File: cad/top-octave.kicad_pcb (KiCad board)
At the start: 2 copper layers, 21 parts, among them J1 DIP-16, U1 ATtiny4-TS, U10 ATtiny4-TS, U11 ATtiny4-TS, U12 ATtiny4-TS, U13 ATtiny4-TS, U2 ATtiny4-TS, U3 ATtiny4-TS, U4 ATtiny4-TS, U5 ATtiny4-TS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

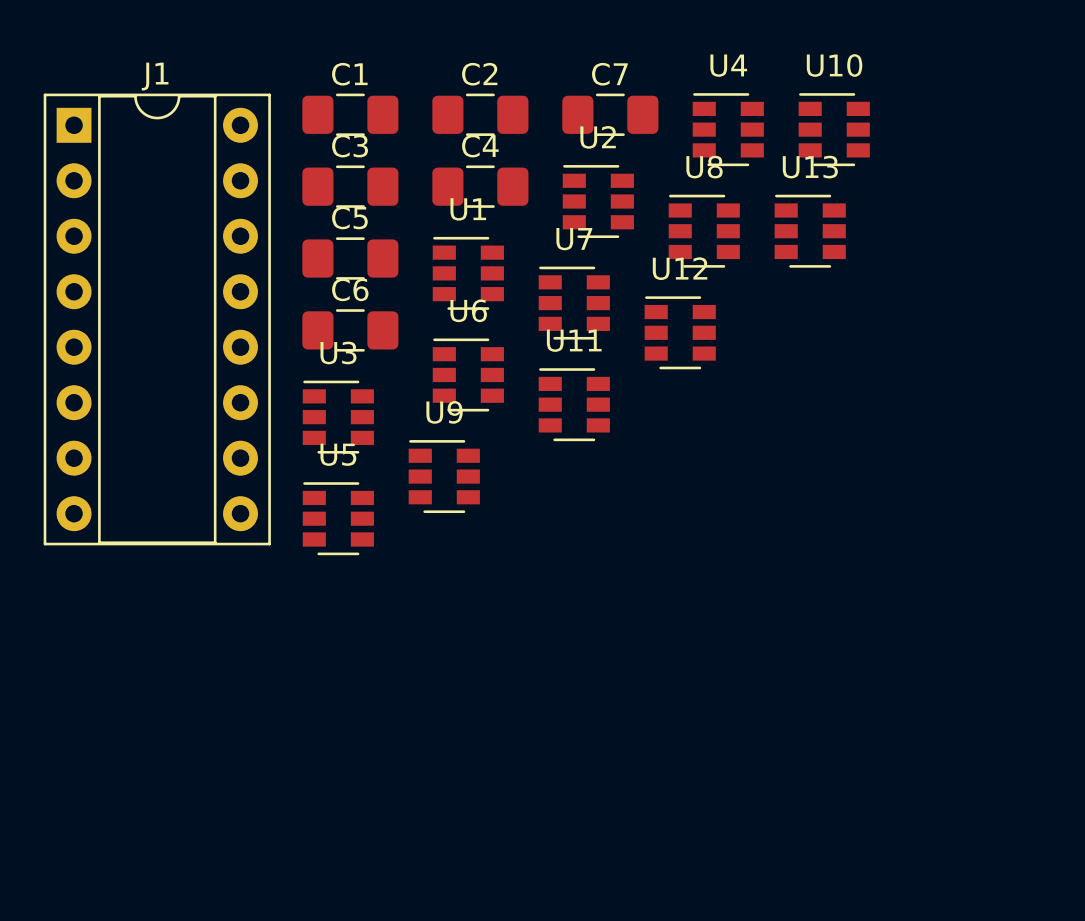
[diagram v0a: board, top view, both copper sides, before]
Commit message: Fix wrong header for MK50242
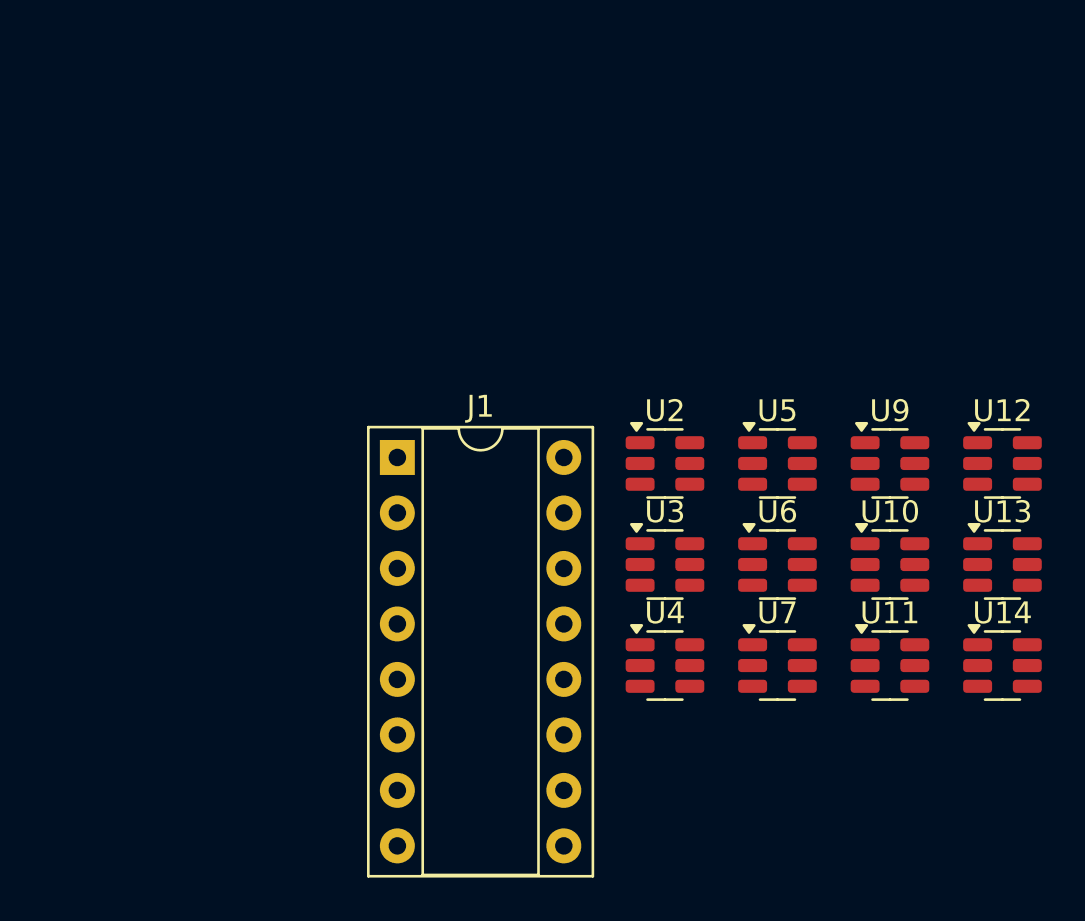
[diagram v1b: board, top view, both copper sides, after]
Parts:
- removed C1, C2, C3, C4, C5, C6, C7: 100n, Capacitor_SMD:C_1206_3216Metric_Pad1.42x1.75mm_HandSolder
- removed U1, U8: ATtiny4-TS, Package_TO_SOT_SMD:SOT-23-6
- added U14: ATtiny4-TS, Package_TO_SOT_SMD:SOT-23-6, F.Cu at (148.2, 86.2)
- moved U4 24.7 mm to (132.8, 86.2)
- moved J1 21.2 mm to (120.5, 76.6)
- moved U9 20.4 mm to (143.1, 76.9)
- moved U5 20.3 mm to (137.9, 76.9)
- moved U10 20.1 mm to (143.1, 81.5)
- moved U7 19.0 mm to (137.9, 86.2)
- moved U11 18.7 mm to (143.1, 86.2)
- moved U13 17.6 mm to (148.2, 81.5)
- moved U6 16.6 mm to (137.9, 81.5)
- moved U3 16.4 mm to (132.8, 81.5)
- moved U12 15.9 mm to (148.2, 76.9)
- moved U2 12.4 mm to (132.8, 76.9)
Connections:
- J1 pad 1: (no net) -> VCC
- J1 pad 10: (no net) -> GND
- J1 pad 11: (no net) -> /DIV_OUT_10
- J1 pad 12: (no net) -> /DIV_OUT_9
- J1 pad 13: (no net) -> /DIV_OUT_6
- J1 pad 14: (no net) -> /DIV_OUT_5
- J1 pad 15: (no net) -> /DIV_OUT_3
- J1 pad 16: (no net) -> /DIV_OUT_1
- J1 pad 2: (no net) -> unconnected-(J1-Pin_2-Pad2)
- J1 pad 3: (no net) -> /DIV_OUT_2
- J1 pad 4: (no net) -> /DIV_OUT_4
- J1 pad 5: (no net) -> /DIV_OUT_7
- J1 pad 6: (no net) -> /DIV_OUT_8
- J1 pad 7: (no net) -> /DIV_OUT_11
- J1 pad 8: (no net) -> /DIV_OUT_12
- J1 pad 9: (no net) -> unconnected-(J1-Pin_9-Pad9)
- U10 pad 1: (no net) -> Net-(Q8-S)
- U10 pad 3: /CLK -> /CLK_C
- U10 pad 4: (no net) -> unconnected-(U10-PB2-Pad4)
- U10 pad 6: /~RESET -> unconnected-(U10-~{RESET}/PB3-Pad6)
- U11 pad 1: (no net) -> Net-(Q9-S)
- U11 pad 3: /CLK -> /CLK_C
- U11 pad 4: (no net) -> unconnected-(U11-PB2-Pad4)
- U11 pad 6: /~RESET -> unconnected-(U11-~{RESET}/PB3-Pad6)
- U12 pad 1: (no net) -> Net-(Q10-S)
- U12 pad 3: /CLK -> /CLK_D
- U12 pad 4: (no net) -> unconnected-(U12-PB2-Pad4)
- U12 pad 6: /~RESET -> unconnected-(U12-~{RESET}/PB3-Pad6)
- U13 pad 1: (no net) -> Net-(Q11-S)
- U13 pad 3: /CLK -> /CLK_D
- U13 pad 4: (no net) -> unconnected-(U13-PB2-Pad4)
- U13 pad 6: /~RESET -> unconnected-(U13-~{RESET}/PB3-Pad6)
- U2 pad 1: (no net) -> Net-(Q1-S)
- U2 pad 3: /CLK -> /CLK_A
- U2 pad 4: (no net) -> unconnected-(U2-PB2-Pad4)
- U2 pad 6: /~RESET -> unconnected-(U2-~{RESET}/PB3-Pad6)
- U3 pad 1: (no net) -> Net-(Q2-S)
- U3 pad 3: /CLK -> /CLK_A
- U3 pad 4: (no net) -> unconnected-(U3-PB2-Pad4)
- U3 pad 6: /~RESET -> unconnected-(U3-~{RESET}/PB3-Pad6)
- U4 pad 1: (no net) -> Net-(Q3-S)
- U4 pad 3: /CLK -> /CLK_A
- U4 pad 4: (no net) -> unconnected-(U4-PB2-Pad4)
- U4 pad 6: /~RESET -> unconnected-(U4-~{RESET}/PB3-Pad6)
- U5 pad 1: (no net) -> Net-(Q4-S)
- U5 pad 3: /CLK -> /CLK_B
- U5 pad 4: (no net) -> unconnected-(U5-PB2-Pad4)
- U5 pad 6: /~RESET -> unconnected-(U5-~{RESET}/PB3-Pad6)
- U6 pad 1: (no net) -> Net-(Q5-S)
- U6 pad 3: /CLK -> /CLK_B
- U6 pad 4: (no net) -> unconnected-(U6-PB2-Pad4)
- U6 pad 6: /~RESET -> unconnected-(U6-~{RESET}/PB3-Pad6)
- U7 pad 1: (no net) -> Net-(Q6-S)
- U7 pad 3: /CLK -> /CLK_B
- U7 pad 4: (no net) -> unconnected-(U7-PB2-Pad4)
- U7 pad 6: /~RESET -> unconnected-(U7-~{RESET}/PB3-Pad6)
- U9 pad 1: (no net) -> Net-(Q7-S)
- U9 pad 3: /CLK -> /CLK_C
- U9 pad 4: (no net) -> unconnected-(U9-PB2-Pad4)
- U9 pad 6: /~RESET -> unconnected-(U9-~{RESET}/PB3-Pad6)
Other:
- net class Default removed

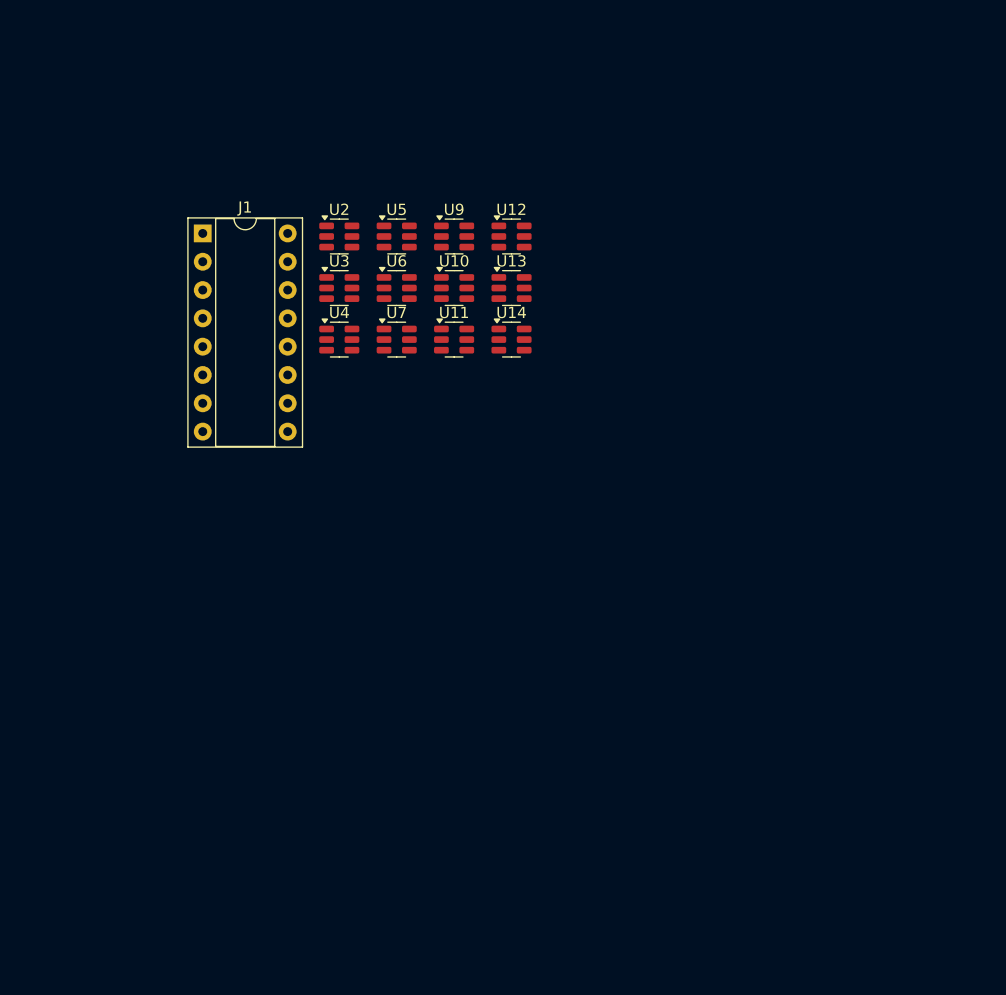
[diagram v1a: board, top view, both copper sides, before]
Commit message: Replace all mosfet by 2 cd4504
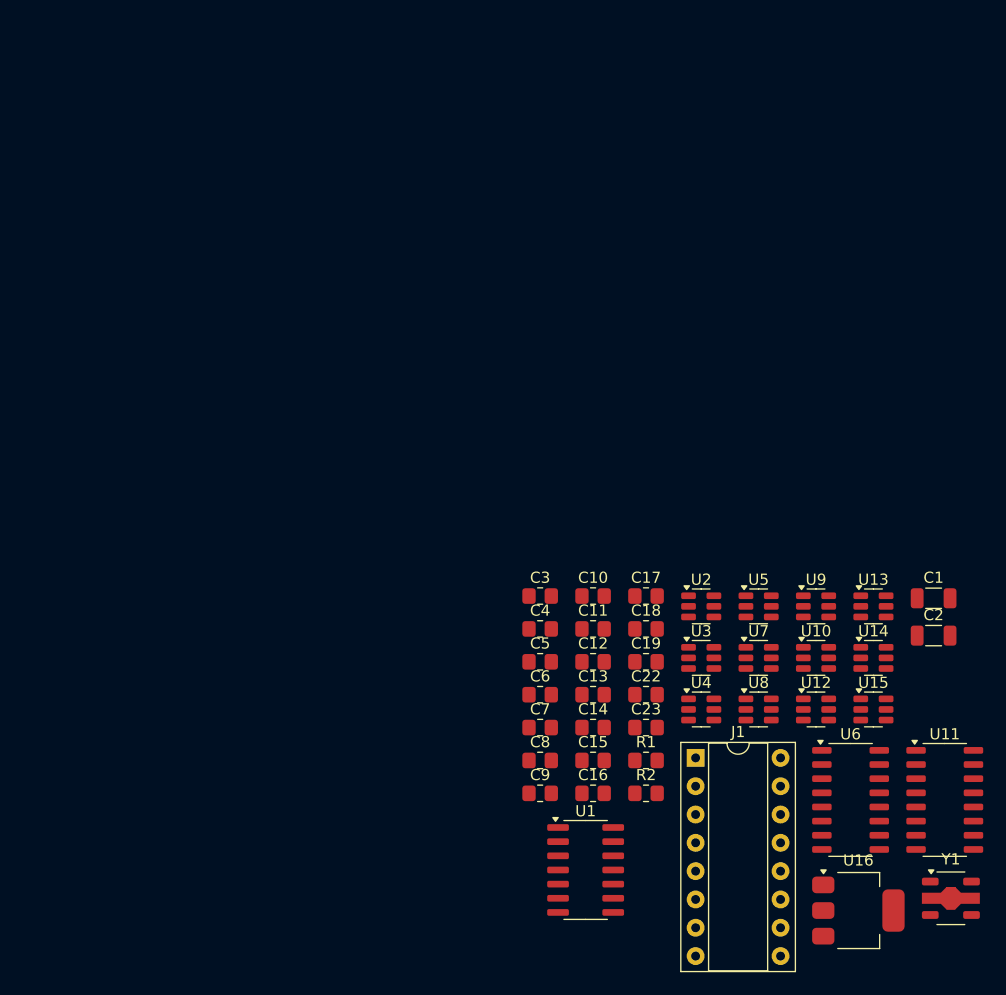
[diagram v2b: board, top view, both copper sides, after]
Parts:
- added C1: 39p, Capacitor_SMD:C_1206_3216Metric, F.Cu at (186.1, 109.4)
- added C10: 100n, Resistor_SMD:R_0805_2012Metric_Pad1.20x1.40mm_HandSolder, F.Cu at (155.5, 109.2)
- added C11: 100n, Resistor_SMD:R_0805_2012Metric_Pad1.20x1.40mm_HandSolder, F.Cu at (155.5, 112.1)
- added C12: 100n, Resistor_SMD:R_0805_2012Metric_Pad1.20x1.40mm_HandSolder, F.Cu at (155.5, 115.1)
- added C13: 100n, Resistor_SMD:R_0805_2012Metric_Pad1.20x1.40mm_HandSolder, F.Cu at (155.5, 118.0)
- added C14: 100n, Resistor_SMD:R_0805_2012Metric_Pad1.20x1.40mm_HandSolder, F.Cu at (155.5, 121.0)
- added C15: 100n, Resistor_SMD:R_0805_2012Metric_Pad1.20x1.40mm_HandSolder, F.Cu at (155.5, 123.9)
- added C16: 100n, Resistor_SMD:R_0805_2012Metric_Pad1.20x1.40mm_HandSolder, F.Cu at (155.5, 126.9)
- added C17: 100n, Resistor_SMD:R_0805_2012Metric_Pad1.20x1.40mm_HandSolder, F.Cu at (160.3, 109.2)
- added C18: 100n, Resistor_SMD:R_0805_2012Metric_Pad1.20x1.40mm_HandSolder, F.Cu at (160.3, 112.1)
- added C19: 100n, Resistor_SMD:R_0805_2012Metric_Pad1.20x1.40mm_HandSolder, F.Cu at (160.3, 115.1)
- added C2: 68p, Capacitor_SMD:C_1206_3216Metric, F.Cu at (186.1, 112.7)
- added C22: 100n, Resistor_SMD:R_0805_2012Metric_Pad1.20x1.40mm_HandSolder, F.Cu at (160.3, 118.0)
- added C23: 100n, Resistor_SMD:R_0805_2012Metric_Pad1.20x1.40mm_HandSolder, F.Cu at (160.3, 121.0)
- added C3: 100n, Resistor_SMD:R_0805_2012Metric_Pad1.20x1.40mm_HandSolder, F.Cu at (150.8, 109.2)
- added C4: 100n, Resistor_SMD:R_0805_2012Metric_Pad1.20x1.40mm_HandSolder, F.Cu at (150.8, 112.1)
- added C5: 100n, Resistor_SMD:R_0805_2012Metric_Pad1.20x1.40mm_HandSolder, F.Cu at (150.8, 115.1)
- added C6: 100n, Resistor_SMD:R_0805_2012Metric_Pad1.20x1.40mm_HandSolder, F.Cu at (150.8, 118.0)
- added C7: 100n, Resistor_SMD:R_0805_2012Metric_Pad1.20x1.40mm_HandSolder, F.Cu at (150.8, 121.0)
- added C8: 100n, Resistor_SMD:R_0805_2012Metric_Pad1.20x1.40mm_HandSolder, F.Cu at (150.8, 123.9)
- added C9: 100n, Resistor_SMD:R_0805_2012Metric_Pad1.20x1.40mm_HandSolder, F.Cu at (150.8, 126.9)
- added R1: 10M, Resistor_SMD:R_0805_2012Metric_Pad1.20x1.40mm_HandSolder, F.Cu at (160.3, 123.9)
- added R2: 4k7, Resistor_SMD:R_0805_2012Metric_Pad1.20x1.40mm_HandSolder, F.Cu at (160.3, 126.9)
- added U1: 74HC04, Package_SO:SOIC-14_3.9x8.7mm_P1.27mm, F.Cu at (154.9, 133.8)
- added U15: ATtiny4-TS, Package_TO_SOT_SMD:SOT-23-6, F.Cu at (180.7, 119.4)
- added U16: uA7805, Package_TO_SOT_SMD:SOT-223, F.Cu at (179.3, 137.4)
- added U8: ATtiny4-TS, Package_TO_SOT_SMD:SOT-23-6, F.Cu at (170.4, 119.4)
- added Y1: 2MHz, Package_TO_SOT_SMD:SOT-89-5, F.Cu at (187.6, 136.3)
- U11, U6: value ATtiny4-TS -> 4504; footprint Package_TO_SOT_SMD:SOT-23-6 -> Package_SO:SO-16_3.9x9.9mm_P1.27mm
- moved J1 64.6 mm to (164.7, 123.7)
- moved U6 61.4 mm to (178.6, 127.5)
- moved U11 60.4 mm to (187.1, 127.5)
- moved U12 50.5 mm to (175.5, 119.4)
- moved U2 46.4 mm to (165.2, 110.1)
- moved U3 46.4 mm to (165.2, 114.7)
- moved U4 46.4 mm to (165.2, 119.4)
- moved U10 46.4 mm to (175.5, 114.7)
- moved U5 46.4 mm to (170.4, 110.1)
- moved U9 46.4 mm to (175.5, 110.1)
- moved U13 43.2 mm to (180.7, 110.1)
- moved U14 43.2 mm to (180.7, 114.7)
- moved U7 43.2 mm to (170.4, 114.7)
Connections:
- U10 pad 1: Net-(Q8-S) -> /OUT_11
- U10 pad 3: /CLK_C -> /CLK_D
- U11 pad 1: Net-(Q9-S) -> +5V
- U11 pad 2: GND -> /DIV_OUT_1
- U11 pad 3: /CLK_C -> /OUT_1
- U11 pad 4: unconnected-(U11-PB2-Pad4) -> /DIV_OUT_3
- U11 pad 5: +5V -> /OUT_3
- U11 pad 6: unconnected-(U11-~{RESET}/PB3-Pad6) -> /DIV_OUT_5
- U12 pad 1: Net-(Q10-S) -> /OUT_3
- U12 pad 3: /CLK_D -> /CLK_A
- U13 pad 1: Net-(Q11-S) -> /OUT_6
- U13 pad 3: /CLK_D -> /CLK_B
- U14 pad 1: Net-(Q12-S) -> /OUT_9
- U14 pad 3: /CLK_D -> /CLK_C
- U2 pad 1: Net-(Q1-S) -> /OUT_1
- U3 pad 1: Net-(Q2-S) -> /OUT_4
- U3 pad 3: /CLK_A -> /CLK_B
- U4 pad 1: Net-(Q3-S) -> /OUT_7
- U4 pad 3: /CLK_A -> /CLK_C
- U5 pad 1: Net-(Q4-S) -> /OUT_10
- U5 pad 3: /CLK_B -> /CLK_D
- U6 pad 1: Net-(Q5-S) -> +5V
- U6 pad 2: GND -> /DIV_OUT_2
- U6 pad 3: /CLK_B -> /OUT_2
- U6 pad 4: unconnected-(U6-PB2-Pad4) -> /DIV_OUT_4
- U6 pad 5: +5V -> /OUT_4
- U6 pad 6: unconnected-(U6-~{RESET}/PB3-Pad6) -> /DIV_OUT_7
- U7 pad 1: Net-(Q6-S) -> /OUT_2
- U7 pad 3: /CLK_B -> /CLK_A
- U9 pad 1: Net-(Q7-S) -> /OUT_8
